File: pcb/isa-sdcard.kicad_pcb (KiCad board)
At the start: 2 copper layers, 123.7 x 73 mm, 34 parts, among them J1 SD Card Board, J3 Bus_ISA_8bit_AB_Rev0, SW1 ADDR SEL, U10 74HC32, U12 74HC165, U13 74HC595, U14 74HC00, U2 74HC00, U22 74HCT688, U4 74HC00, U5 74HC163, U6 74HCT138, U7 74HC123, U9 74HC32, X1 16MHz

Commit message: Revising schematics and layout
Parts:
- removed the C1 at (117.1, 101.5)
- removed C20, C21: 22pF, Capacitor_THT:C_Disc_D5.0mm_W2.5mm_P5.00mm
- removed C25: 0.1uF, Capacitor_THT:C_Disc_D5.0mm_W2.5mm_P5.00mm
- removed the C5 at (150.9, 85.3)
- removed R3: 10k, Resistor_THT:R_Axial_DIN0207_L6.3mm_D2.5mm_P7.62mm_Horizontal
- removed R5: 1k, Resistor_THT:R_Axial_DIN0207_L6.3mm_D2.5mm_P7.62mm_Horizontal
- removed U10, U9: 74HC32, Package_DIP:DIP-14_W7.62mm_Socket
- removed the U4 at (122.2, 61.2)
- removed the U6 at (93.0, 101.5)
- removed the U7 at (66.4, 75.2)
- added U2: 74HCT32, Package_DIP:DIP-14_W7.62mm_Socket, F.Cu at (119.6, 89.1)
- added U3: 74HCT139, Package_DIP:DIP-16_W7.62mm_Socket, F.Cu at (117.1, 101.8)
- J1: value SD Card Board -> SDCARD
- U6: renamed from U12; value 74HC165 -> 74HCT165
- U7: renamed from U13; value 74HC595 -> 74HCT595
- moved SW1 71.2 mm to (84.1, 101.8)
- moved RN1 68.6 mm to (104.4, 106.9)
- moved J1 65.5 mm to (142.5, 66.3), turned to 180 degrees
- moved C3 47.8 mm to (114.5, 87.9)
- moved C4 47.5 mm to (112.0, 100.5)
- moved U8 45.3 mm to (79.0, 89.1)
- moved U4 41.3 mm to (82.8, 76.4)
- moved U5 38.7 mm to (119.6, 63.7)
- moved C5 37.9 mm to (143.7, 100.5)
- moved C6 36.9 mm to (143.7, 85.3)
- moved X1 31.8 mm to (99.3, 54.9), turned to 180 degrees
- moved U7 28.5 mm to (150.1, 101.8)
- moved C1 27.1 mm to (77.7, 75.2)
- moved C9 26.2 mm to (114.5, 75.1)
- moved C2 25.2 mm to (114.5, 62.5)
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- renumbered C2 to C1, C24 to C10, C3 to C2, C23 to C3, C6 to C5, C7 to C6, C8 to C7, C27 to C8, C26 to C9, J3 to J2, R4 to R1, RN2 to RN1, U2 to U1, U5 to U4, U14 to U5, U22 to U8
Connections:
- net SD_SPI renamed Net-(U4-~{MR})
- C1 pad 2: +5V -> VCC
- C10 pad 1: +5V -> VCC
- C2 pad 2: +5V -> VCC
- C3 pad 2: +5V -> VCC
- C4 pad 2: +5V -> VCC
- C5 pad 2: +5V -> VCC
- C6 pad 2: +5V -> VCC
- C7 pad 1: +5V -> VCC
- C8 pad 2: +5V -> VCC
- C9 pad 2: +5V -> VCC
- J1 pad 5: +5V -> VCC
- J2 pad B02: RESET -> unconnected-(J2-RESET-PadB02)
- J2 pad B03: +5V -> VCC
- J2 pad B29: +5V -> VCC
- RN1 pad 2: Net-(RN2-R1) -> Net-(RN1-R1)
- RN1 pad 3: Net-(RN2-R2) -> Net-(RN1-R2)
- RN1 pad 4: Net-(RN2-R3) -> Net-(RN1-R3)
- RN1 pad 5: Net-(RN2-R4) -> Net-(RN1-R4)
- RN1 pad 6: Net-(RN2-R5) -> Net-(RN1-R5)
- RN1 pad 7: Net-(RN2-R6) -> Net-(RN1-R6)
- RN1 pad 8: Net-(RN2-R7) -> Net-(RN1-R7)
- RN1 pad 9: unconnected-(RN2-R8-Pad9) -> Net-(RN1-R8)
- SW1 pad 1: Net-(RN2-R7) -> Net-(RN1-R8)
- SW1 pad 10: +5V -> VCC
- SW1 pad 11: +5V -> VCC
- SW1 pad 12: +5V -> VCC
- SW1 pad 13: +5V -> VCC
- SW1 pad 14: +5V -> VCC
- SW1 pad 15: +5V -> VCC
- SW1 pad 16: +5V -> VCC
- SW1 pad 2: Net-(RN2-R6) -> Net-(RN1-R7)
- SW1 pad 3: Net-(RN2-R5) -> Net-(RN1-R6)
- SW1 pad 4: Net-(RN2-R4) -> Net-(RN1-R5)
- SW1 pad 5: Net-(RN2-R3) -> Net-(RN1-R4)
- SW1 pad 6: Net-(RN2-R2) -> Net-(RN1-R3)
- SW1 pad 7: Net-(RN2-R1) -> Net-(RN1-R2)
- SW1 pad 8: unconnected-(SW1-Pad8) -> Net-(RN1-R1)
- SW1 pad 9: unconnected-(SW1-Pad9) -> VCC
- U1 pad 14: +5V -> VCC
- U1 pad 5: ~{CLKSTART_DB} -> ~{CLKSTART}
- U4 pad 10: +5V -> VCC
- U4 pad 16: +5V -> VCC
- U4 pad 7: +5V -> VCC
- U4 pad 9: +5V -> VCC
- U5 pad 14: +5V -> VCC
- U6 pad 10: +5V -> VCC
- U6 pad 16: +5V -> VCC
- U7 pad 10: +5V -> VCC
- U7 pad 16: +5V -> VCC
- U8 pad 11: A7 -> A6
- U8 pad 12: Net-(RN2-R5) -> Net-(RN1-R5)
- U8 pad 13: A8 -> A7
- U8 pad 14: Net-(RN2-R6) -> Net-(RN1-R6)
- U8 pad 15: A9 -> A8
- U8 pad 16: Net-(RN2-R7) -> Net-(RN1-R7)
- U8 pad 17: GND -> A9
- U8 pad 18: GND -> Net-(RN1-R8)
- U8 pad 2: A3 -> A2
- U8 pad 20: +5V -> VCC
- U8 pad 3: Net-(RN2-R1) -> Net-(RN1-R1)
- U8 pad 4: A4 -> A3
- U8 pad 5: Net-(RN2-R2) -> Net-(RN1-R2)
- U8 pad 6: A5 -> A4
- U8 pad 7: Net-(RN2-R3) -> Net-(RN1-R3)
- U8 pad 8: A6 -> A5
- U8 pad 9: Net-(RN2-R4) -> Net-(RN1-R4)
- X1 pad 14: +5V -> VCC
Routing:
- net GND: track 945.0 -> 102.3 mm, vias 1 -> 0
- net +5V: track 607.5 -> 0.00 mm, vias 4 -> 0
- net ~{CS}: track 124.5 -> 24.5 mm, vias 1 -> 0
- net VCC: track 0.00 -> 97.5 mm
- net ~{WR}: track 103.5 -> 29.2 mm
- net MOSI: track 106.5 -> 40.2 mm
- net MISO: track 107.6 -> 47.7 mm, vias 1 -> 2
- net A7: track 59.7 -> 0.00 mm, vias 1 -> 0
- net A6: track 55.6 -> 0.00 mm, vias 1 -> 0
- net A5: track 55.5 -> 0.00 mm
- net ~{SER_WR}: track 80.3 -> 28.1 mm, vias 2 -> 1
- net A8: track 52.1 -> 0.00 mm, vias 1 -> 0
- net D2: track 105.2 -> 54.0 mm
- net A4: track 50.7 -> 0.00 mm
- net Net-(RN2-R1): track 50.6 -> 0.00 mm
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- added copper zone on B.Cu, net VCC
- removed copper zone on B.Cu, net GND

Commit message: Revising design
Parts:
- added J3: Conn_01x05_Pin, Connector_PinHeader_2.54mm:PinHeader_1x05_P2.54mm_Vertical, F.Cu at (129.8, 49.8)
- added TP1: ~{CS}, TestPoint:TestPoint_Loop_D3.80mm_Drill2.0mm, F.Cu at (61.2, 90.4)
- added TP2: CLK, TestPoint:TestPoint_Loop_D3.80mm_Drill2.0mm, F.Cu at (61.2, 81.5)
- added TP3: MOSI, TestPoint:TestPoint_Loop_D3.80mm_Drill2.0mm, F.Cu at (61.2, 72.6)
- added TP4: MISO, TestPoint:TestPoint_Loop_D3.80mm_Drill2.0mm, F.Cu at (61.2, 63.7)
- added TP5: MISO, TestPoint:TestPoint_Loop_D3.80mm_Drill2.0mm, F.Cu at (61.2, 54.9)
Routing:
- net MOSI: track 40.2 -> 137.4 mm
- net MISO: track 47.7 -> 139.5 mm
- net ~{CS}: track 24.5 -> 108.4 mm
- net AEN: track 40.2 -> 99.6 mm, vias 1 -> 4
- net Net-(RN1-R5): track 5.08 -> 59.8 mm
- net A9: track 0.00 -> 49.6 mm, vias 0 -> 4
- net A0: track 12.3 -> 61.4 mm, vias 0 -> 1
- net CLKSTOP: track 0.00 -> 49.0 mm
- net A1: track 11.7 -> 60.3 mm, vias 0 -> 1
- net CLK: track 112.1 -> 160.7 mm
- net Net-(RN1-R6): track 5.08 -> 52.2 mm, vias 0 -> 1
- net Net-(RN1-R3): track 5.08 -> 50.9 mm
- net A8: track 0.00 -> 42.7 mm, vias 0 -> 2
- net Net-(RN1-R2): track 5.08 -> 44.7 mm, vias 0 -> 2
- net A6: track 0.00 -> 37.9 mm
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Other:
- board text added: "A2"
- board text added: "CLK"
- board text added: "GND"
- board text added: "MISO"
- board text added: "MOSI"
- board text added: "jlcjlcjlcjlc"
- board text added: "~{CS}"

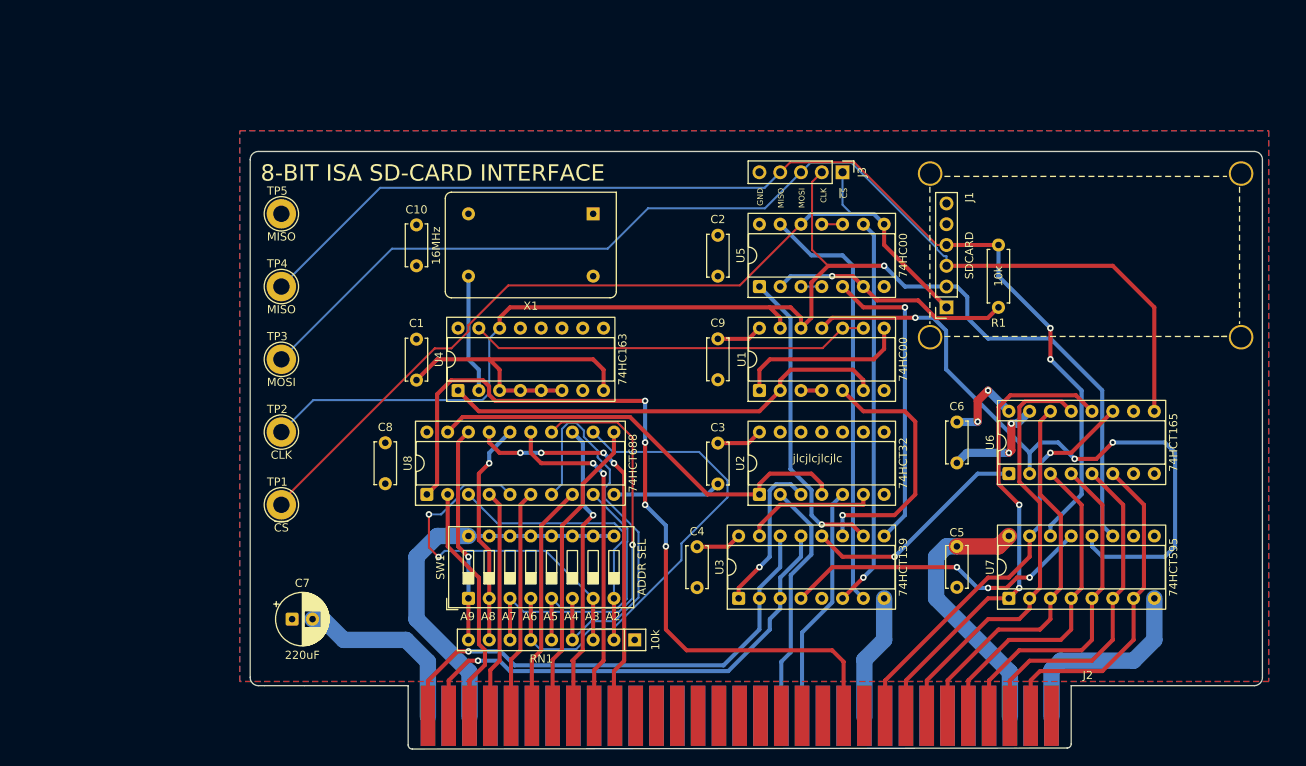
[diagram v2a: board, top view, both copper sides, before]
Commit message: Revising lay-out
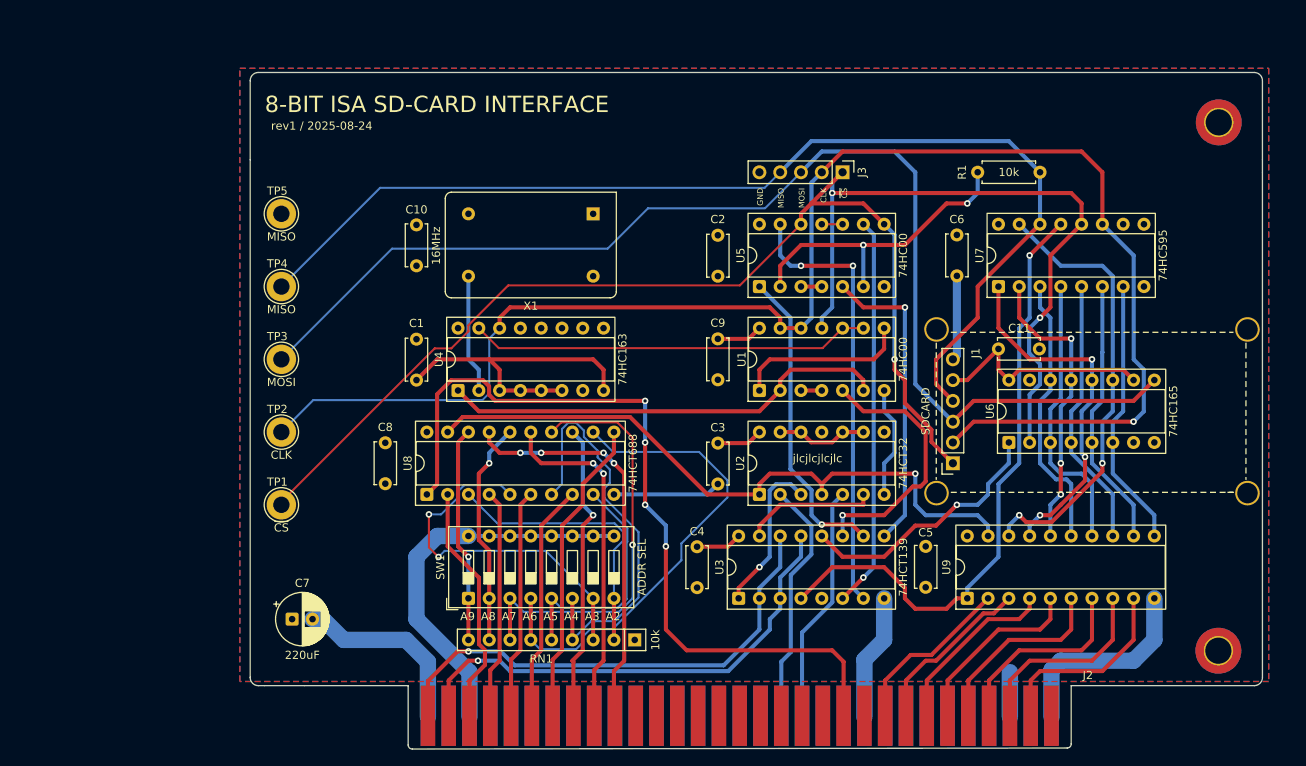
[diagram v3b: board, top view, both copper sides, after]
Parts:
- added C11: 0.1uF, Capacitor_THT:C_Disc_D5.0mm_W2.5mm_P5.00mm, F.Cu at (153.8, 71.4)
- added H1: MountingHole_Pad, MountingHole:MountingHole_3.2mm_M3_DIN965_Pad_TopBottom, F.Cu at (175.7, 43.7)
- added H2: MountingHole_Pad, MountingHole:MountingHole_3.2mm_M3_DIN965_Pad_TopBottom, F.Cu at (175.7, 108.2)
- added U9: 74HCT245, Package_DIP:DIP-20_W7.62mm_Socket, F.Cu at (145.0, 101.8)
- U6: value 74HCT165 -> 74HC165
- U7: value 74HCT595 -> 74HC595
- moved U7 38.1 mm to (148.8, 63.7)
- moved C6 22.9 mm to (143.7, 62.4)
- moved J1 19.1 mm to (143.3, 85.3)
- moved R1 16.7 mm to (146.3, 49.8), turned to 0 degrees
- moved C5 3.81 mm to (139.9, 100.5)
- moved U6 3.81 mm to (150.1, 82.8)
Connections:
- J2 pad A02: D7 -> DB7
- J2 pad A03: D6 -> DB6
- J2 pad A04: D5 -> DB5
- J2 pad A05: D4 -> DB4
- J2 pad A06: D3 -> DB3
- J2 pad A07: D2 -> DB2
- J2 pad A08: D1 -> DB1
- J2 pad A09: D0 -> DB0
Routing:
- net ~{SER_RD}: track 38.3 -> 75.7 mm, vias 3 -> 1
- net CLK: track 160.7 -> 189.0 mm
- net ~{PORTSEL}: track 54.0 -> 81.0 mm, vias 0 -> 1
- net DB7: track 0.00 -> 24.1 mm
- net DB5: track 0.00 -> 24.1 mm
- net DB6: track 0.00 -> 24.1 mm
- net DB4: track 0.00 -> 23.4 mm
- net DB3: track 0.00 -> 22.7 mm
- net GND: track 128.9 -> 150.9 mm, vias 2 -> 0
- net DB2: track 0.00 -> 21.9 mm
- net DB1: track 0.00 -> 21.2 mm
- net DB0: track 0.00 -> 21.2 mm
- net ~{CS}: track 108.4 -> 129.1 mm, vias 0 -> 1
- net D2: track 54.0 -> 36.4 mm, vias 0 -> 3
- net D1: track 58.9 -> 43.9 mm, vias 2 -> 3
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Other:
- board size 123.7 x 73 mm -> 123.7 x 82.7 mm
- board text added: "rev1 / 2025-08-24"

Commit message: Revising PCB and adding source code
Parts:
- TP5: value MISO -> GND
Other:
- board text added: "rev2 / 2025-09-06"
- board text removed: "rev1 / 2025-08-24"

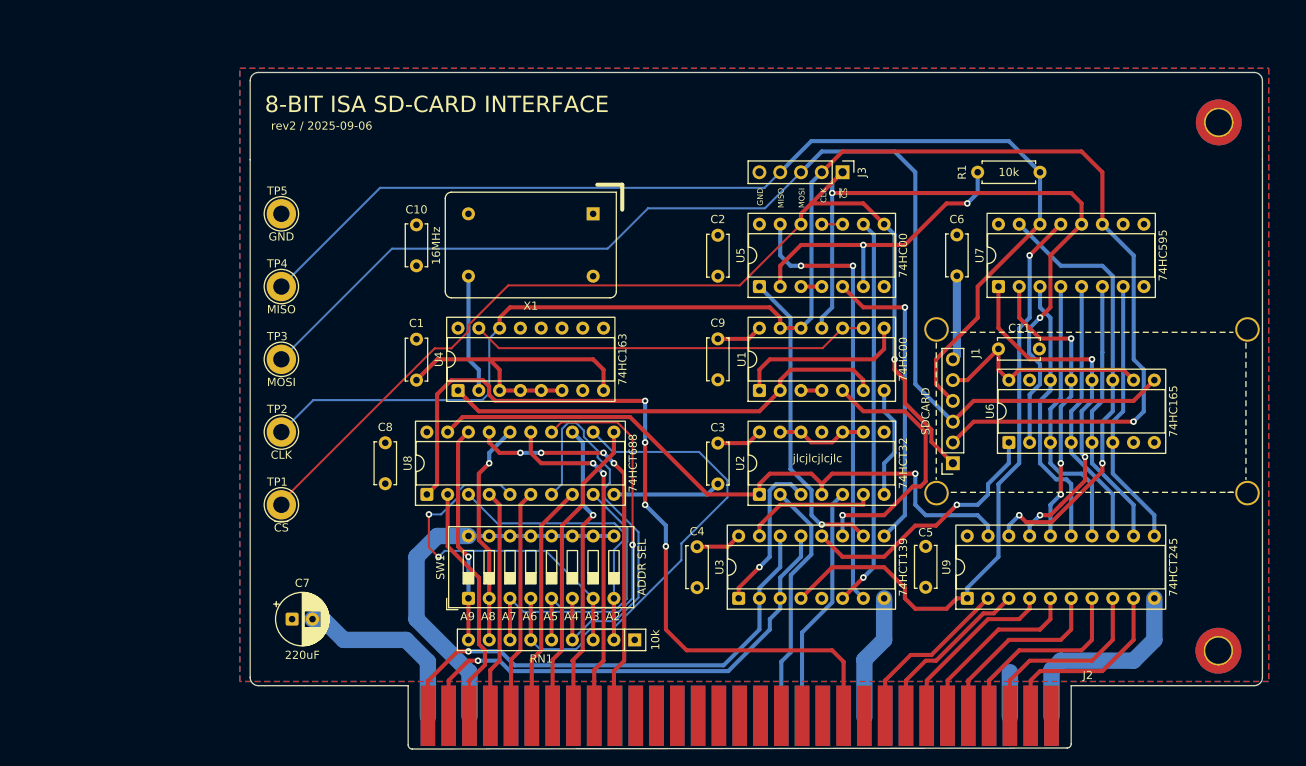
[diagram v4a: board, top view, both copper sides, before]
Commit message: Expanding PCB and adding reading directory to firmware
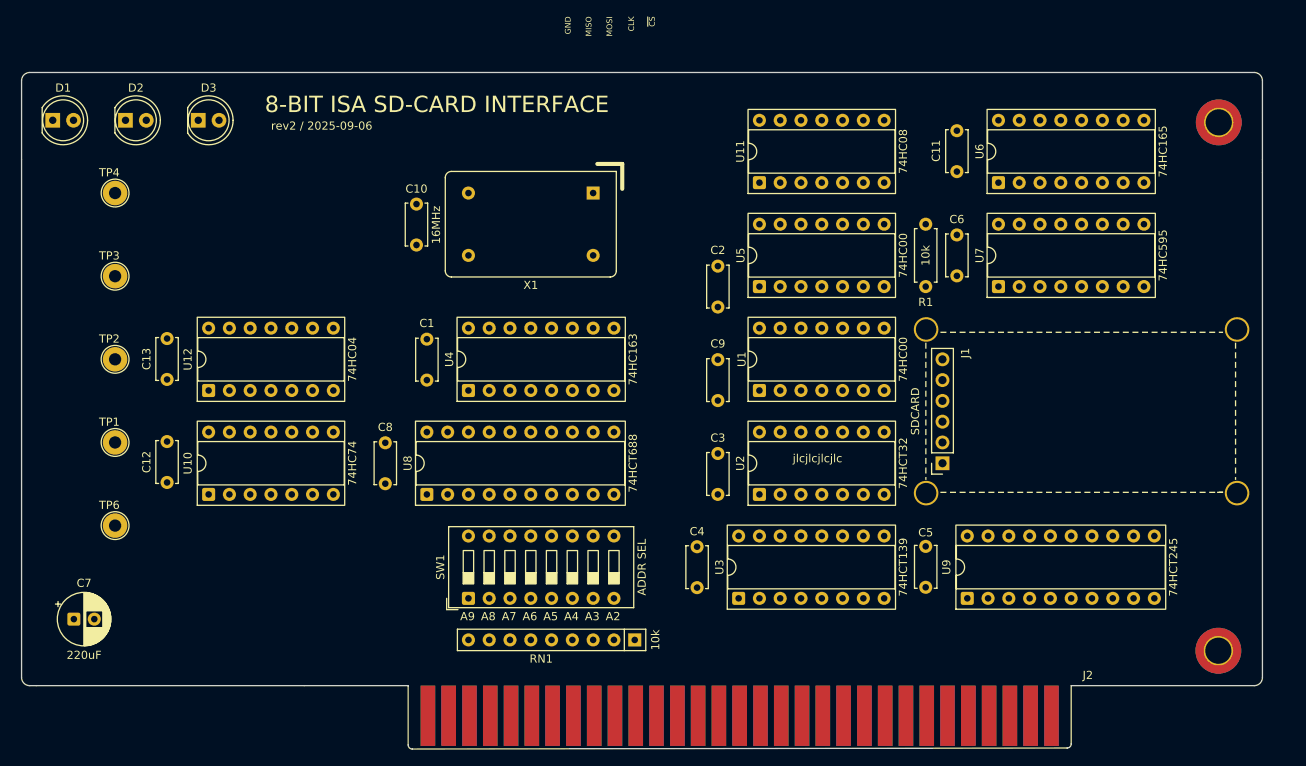
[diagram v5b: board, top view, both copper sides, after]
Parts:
- removed J3: Conn_01x05_Pin, Connector_PinHeader_2.54mm:PinHeader_1x05_P2.54mm_Vertical
- removed TP5: GND, TestPoint:TestPoint_Loop_D3.80mm_Drill2.0mm
- added C12: 0.1uF, Capacitor_THT:C_Disc_D5.0mm_W2.5mm_P5.00mm, F.Cu at (47.2, 87.7)
- added C13: 0.1uF, Capacitor_THT:C_Disc_D5.0mm_W2.5mm_P5.00mm, F.Cu at (47.2, 75.1)
- added D1: LED, LED_THT:LED_D5.0mm, F.Cu at (33.3, 43.4)
- added D2: LED, LED_THT:LED_D5.0mm, F.Cu at (42.1, 43.4)
- added D3: LED, LED_THT:LED_D5.0mm, F.Cu at (51.0, 43.4)
- added TP6: ~{Q}, TestPoint:TestPoint_Loop_D2.54mm_Drill1.5mm_Beaded, F.Cu at (40.9, 93.0)
- added U10: 74HC74, Package_DIP:DIP-14_W7.62mm_Socket, F.Cu at (52.3, 89.1)
- added U11: 74HC08, Package_DIP:DIP-14_W7.62mm_Socket, F.Cu at (119.6, 51.0)
- added U12: 74HC04, Package_DIP:DIP-14_W7.62mm_Socket, F.Cu at (52.3, 76.4)
- TP1, TP2, TP3, TP4: footprint TestPoint:TestPoint_Loop_D3.80mm_Drill2.0mm -> TestPoint:TestPoint_Loop_D2.54mm_Drill1.5mm_Beaded
- moved U6 31.8 mm to (148.8, 51.0)
- moved C11 28.5 mm to (143.7, 44.7), turned to -90 degrees
- moved C7 26.7 mm to (35.8, 104.4)
- moved TP4 23.3 mm to (40.9, 52.3)
- moved TP3 22.7 mm to (40.9, 62.5)
- moved TP2 22.2 mm to (40.9, 72.6)
- moved TP1 21.7 mm to (40.9, 82.8)
- moved R1 15.3 mm to (139.9, 63.7), turned to 90 degrees
- moved C2 3.77 mm to (114.5, 66.2)
- moved C10 2.54 mm to (77.7, 58.7)
- moved C9 2.54 mm to (114.5, 77.7)
- moved X1 2.54 mm to (99.3, 52.3)
- moved U4 1.27 mm to (84.1, 76.4)
- moved C1 1.27 mm to (79.0, 75.2)
- moved C3 1.27 mm to (114.5, 89.1)
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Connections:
- U3 pad 11: ~{CLKSTART} -> ~{PULSE}
- U3 pad 4: ~{SER_RD} -> ~{RQ_SER_RD}
- U3 pad 5: unconnected-(U3A-O1-Pad5) -> ~{SER_RD_AND_PULSE}
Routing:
- net CLK: track 189.0 -> 0.00 mm, vias 1 -> 0
- net GND: track 150.9 -> 0.00 mm
- net MOSI: track 149.8 -> 0.00 mm
- net MISO: track 135.7 -> 0.00 mm
- net ~{CS}: track 129.1 -> 0.00 mm, vias 1 -> 0
- net AEN: track 99.6 -> 0.00 mm, vias 4 -> 0
- net VCC: track 97.5 -> 0.00 mm
- net ~{CLK}: track 83.5 -> 0.00 mm, vias 2 -> 0
- net ~{PORTSEL}: track 81.0 -> 0.00 mm, vias 1 -> 0
- net ~{SER_RD}: track 75.7 -> 0.00 mm, vias 1 -> 0
- net A0: track 61.4 -> 0.00 mm, vias 1 -> 0
- net A1: track 60.3 -> 0.00 mm, vias 1 -> 0
- net Net-(RN1-R5): track 59.8 -> 0.00 mm
- net Net-(U4-~{MR}): track 55.2 -> 0.00 mm
- net D0: track 54.6 -> 0.00 mm, vias 2 -> 0
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- removed copper zone on F.Cu, net GND
- removed copper zone on B.Cu, net VCC
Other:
- board size 123.7 x 82.7 mm -> 151.6 x 82.7 mm
